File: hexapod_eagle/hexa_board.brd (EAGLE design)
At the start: 80 x 90 mm, 68 parts, among them X1 ARK2, X2 ARK1

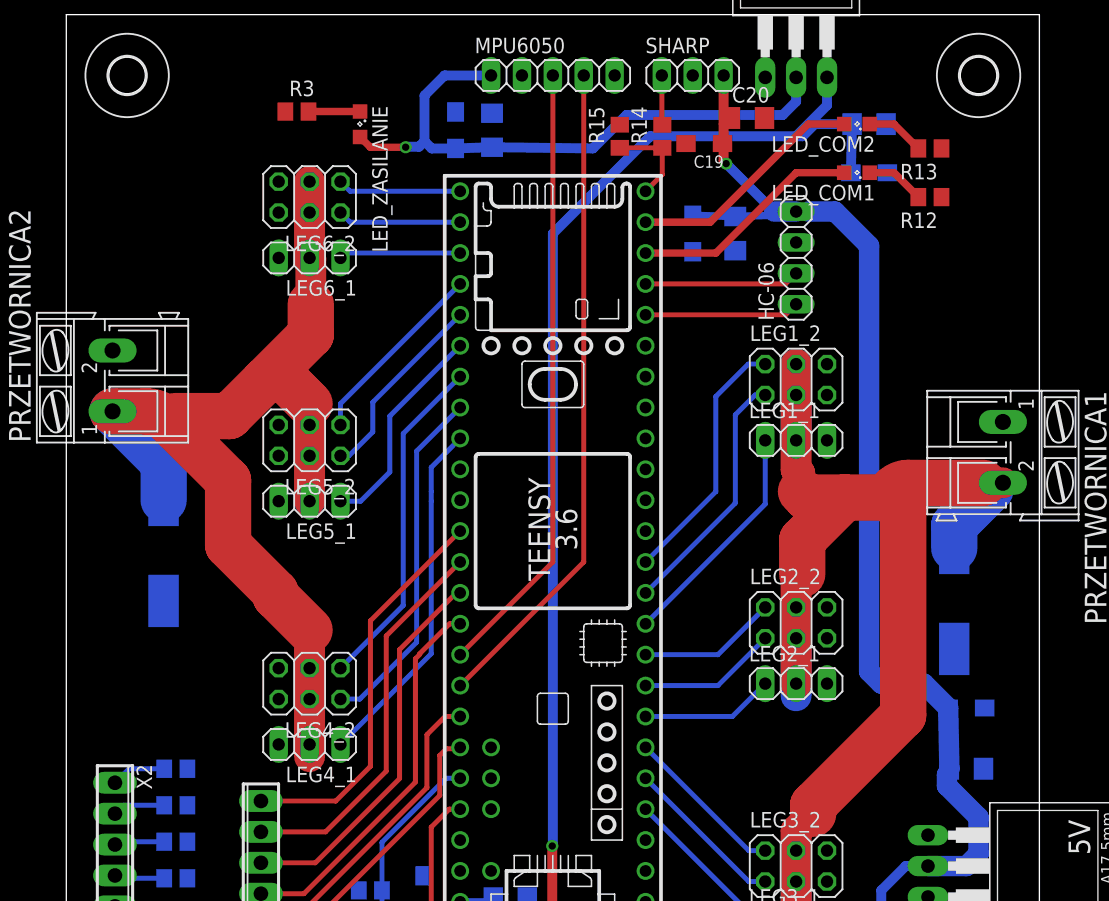
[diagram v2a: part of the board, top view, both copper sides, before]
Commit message: Update eagle files
-change positions some capacitors
-change TXD/RXD lines
-minor changes
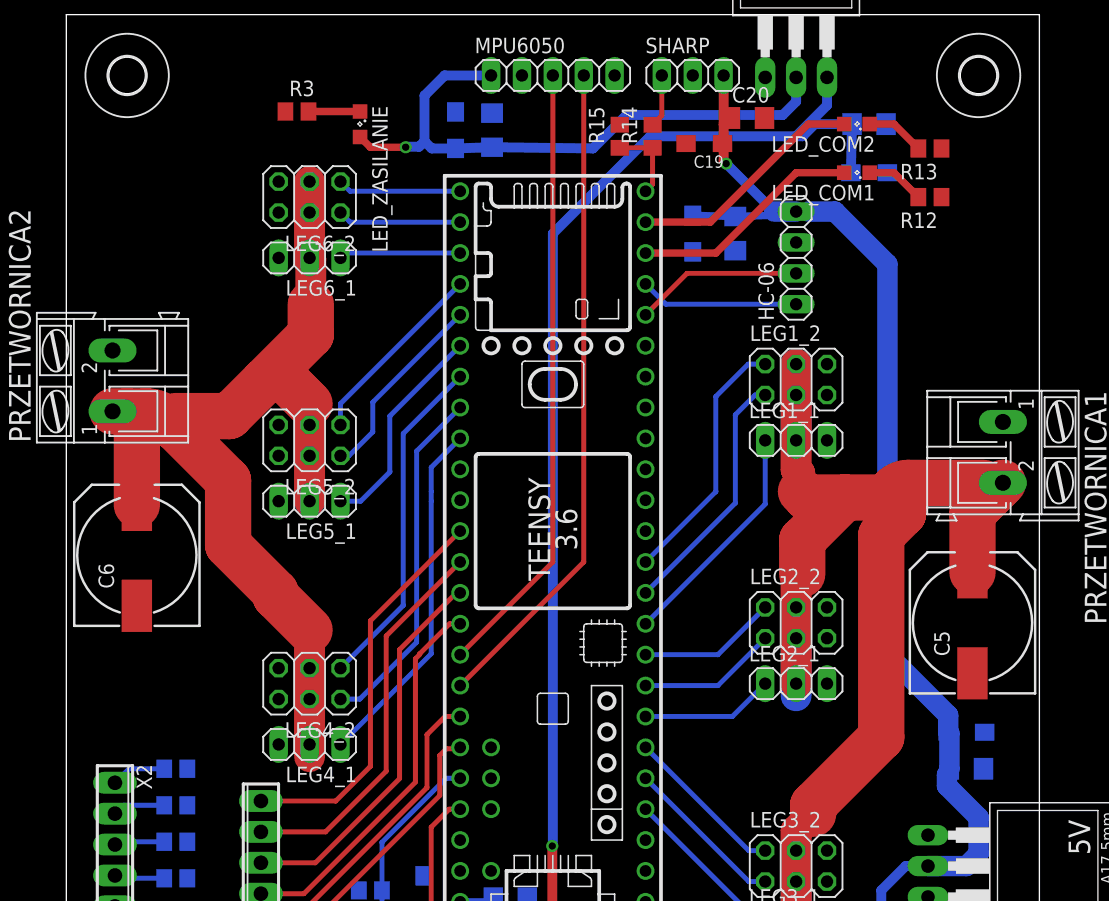
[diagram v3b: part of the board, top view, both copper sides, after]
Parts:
- moved C5 2.50 mm to (34.5, -5.00), flipped to the top
- moved C6 2.24 mm to (-34.2, 0.55), flipped to the top
- moved C4 2.00 mm to (34.0, -14.0)
- moved R14 0.80 mm to (8.20, 35.0)
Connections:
- net RXD7: now also TEENSY41.28; no longer TEENSY41.29
- net TXD7: now also TEENSY41.29; no longer TEENSY41.28
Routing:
- net +6V1: track 146.8 -> 149.1 mm
- net +5V: track 118.7 -> 116.7 mm
- net SENSOR: track 7.64 -> 6.51 mm
- net RXD7: track 12.7 -> 13.8 mm
- net +6V2: track 104.7 -> 103.6 mm
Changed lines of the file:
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@@
 <grid distance="1" unitdist="mm" unit="mm" style="lines" multiple="1" display="no" altdistance="0.05" altunitdist="mm" altunit="mm"/>
 <layers>
-<layer number="1" name="Top" color="4" fill="1" visible="yes" active="yes"/>
+<layer number="1" name="Top" color="4" fill="1" visible="no" active="yes"/>
 <layer number="2" name="Route2" color="1" fill="3" visible="no" active="no"/>
 <layer number="3" name="Route3" color="4" fill="3" visible="no" active="no"/>
@@
 <element name="C2" library="rcl" package="C1206" value="10uF" x="34" y="-31"/>
 <element name="C3" library="rcl" package="C1206" value="10uF" x="34" y="-17" rot="MR180"/>
-<element name="C4" library="rcl" package="SMC_A" value="100n" x="34" y="-12" rot="MR180"/>
+<element name="C4" library="rcl" package="SMC_A" value="100n" x="34" y="-14" rot="MR180"/>
 <element name="HC-06" library="pinhead" package="1X04" value="" x="20" y="25" rot="R90"/>
 <element name="R1" library="rcl" package="R0805" value="510r" x="-8" y="-33"/>
@@
 <attribute name="OC_FARNELL" value="unknown" x="-36" y="-24.5" size="1.778" layer="27" rot="R270" display="off"/>
 </element>
-<element name="C5" library="rcl" package="150CLZ-1014" value="" x="33" y="-3" rot="MR90"/>
-<element name="C6" library="rcl" package="150CLZ-1014" value="" x="-32" y="0.95" rot="MR90"/>
+<element name="C5" library="rcl" package="150CLZ-1014" value="" x="34.5" y="-5" rot="R90"/>
+<element name="C6" library="rcl" package="150CLZ-1014" value="" x="-34.2" y="0.55" rot="R90"/>
 <element name="WLACZNIK1" library="switch" package="255SB" value="7.2V" x="16" y="-41.7"/>
 <element name="C11" library="rcl" package="SMC_A" value="100n" x="-10.6" y="-27.3" rot="MR90"/>
@@
 <element name="C15" library="rcl" package="SMC_A" value="100n" x="11.5" y="27" rot="MR270"/>
 <element name="C16" library="rcl" package="C1206" value="10uF" x="15" y="27" rot="MR270"/>
-<element name="R14" library="rcl" package="R0805" value="510r" x="9" y="35" rot="R90"/>
+<element name="R14" library="rcl" package="R0805" value="510r" x="8.2" y="35" rot="R90"/>
 <element name="R15" library="rcl" package="R0805" value="510r" x="5.5" y="35" rot="R90"/>
 <element name="C17" library="rcl" package="C1206" value="10uF" x="20.45" y="-37.25" rot="MR225"/>
@@
 <wire x1="20" y1="-22.1" x2="21.4" y2="-20.7" width="2.54" layer="1"/>
 <wire x1="21.4" y1="-20.7" x2="21.4" y2="-20" width="3.81" layer="1"/>
-<wire x1="21.4" y1="-20" x2="28.8" y2="-12.6" width="3.81" layer="1"/>
-<wire x1="28.8" y1="-12.6" x2="28.8" y2="4" width="3.81" layer="1"/>
 <wire x1="28.8" y1="4" x2="28.8" y2="4.8" width="3.81" layer="1"/>
 <wire x1="28.8" y1="4.8" x2="29" y2="5" width="3.81" layer="1"/>
@@
 <wire x1="28.74395" y1="4.05605" x2="28.8" y2="4" width="3.81" layer="1"/>
 <contactref element="C5" pad="+"/>
-<wire x1="33" y1="1.15" x2="33" y2="3" width="3.81" layer="16"/>
-<wire x1="33" y1="3" x2="36" y2="6" width="3.81" layer="16"/>
-<wire x1="35.426075" y1="6.5108" x2="36" y2="6" width="0" layer="19" extent="1-16"/>
+<wire x1="28.8" y1="4" x2="27" y2="2.2" width="3.81" layer="1"/>
+<wire x1="27" y1="2.2" x2="27" y2="-14.4" width="3.81" layer="1"/>
+<wire x1="21.4" y1="-20" x2="27" y2="-14.4" width="3.81" layer="1"/>
+<wire x1="37" y1="6.5108" x2="34.5" y2="4.0108" width="3.81" layer="1"/>
+<wire x1="34.5" y1="4.0108" x2="34.5" y2="-0.85" width="3.81" layer="1"/>
 </signal>
 <signal name="+6V2">
@@
 <wire x1="-19.9" y1="24.9" x2="-20" y2="25" width="2.54" layer="1"/>
 <contactref element="PRZETWORNICA2" pad="1"/>
-<wire x1="-36.2" y1="12.3854" x2="-33.437503125" y2="12.3854" width="3.81" layer="1"/>
+<wire x1="-36.2" y1="12.3854" x2="-35" y2="12.3854" width="3.81" layer="1"/>
+<wire x1="-35" y1="12.3854" x2="-33.437503125" y2="12.3854" width="3.81" layer="1"/>
 <wire x1="-33.437503125" y1="12.3854" x2="-31.64145" y2="11.64145" width="3.81" layer="1" curve="-45.00005"/>
 <wire x1="-31.64145" y1="11.64145" x2="-31" y2="11" width="3.81" layer="1"/>
 <contactref element="C6" pad="+"/>
-<wire x1="-32" y1="5.1" x2="-32" y2="8.1854" width="3.81" layer="16"/>
-<wire x1="-32" y1="8.1854" x2="-36.2" y2="12.3854" width="3.81" layer="16"/>
+<wire x1="-34.2" y1="4.7" x2="-34.2" y2="11.5854" width="3.81" layer="1"/>
+<wire x1="-34.2" y1="11.5854" x2="-35" y2="12.3854" width="3.81" layer="1"/>
 </signal>
 <signal name="SDA">
@@
 <wire x1="21" y1="28.81" x2="23.19" y2="28.81" width="1.6764" layer="16"/>
 <contactref element="5V" pad="2"/>
-<wire x1="32.5" y1="-12" x2="32.6" y2="-17" width="1.6764" layer="16"/>
 <contactref element="SHARP" pad="3"/>
 <wire x1="14.04" y1="40" x2="14.04" y2="36" width="0.8128" layer="1"/>
@@
 <wire x1="32.4" y1="-17.5" x2="32.5" y2="-17.4" width="1.6764" layer="16"/>
 <wire x1="32.5" y1="-17.4" x2="32.6" y2="-17" width="1.6764" layer="16"/>
-<wire x1="32.5" y1="-12" x2="30.5" y2="-10" width="1.6764" layer="16"/>
-<wire x1="30.5" y1="-10" x2="27" y2="-10" width="1.6764" layer="16"/>
-<wire x1="27" y1="-10" x2="26" y2="-9" width="1.6764" layer="16"/>
-<wire x1="26" y1="-9" x2="26" y2="26" width="1.6764" layer="16"/>
-<wire x1="26" y1="26" x2="23.19" y2="28.81" width="1.6764" layer="16"/>
+<wire x1="27.5" y1="24.5" x2="23.19" y2="28.81" width="1.6764" layer="16"/>
 <contactref element="WLACZNIK1" pad="2"/>
 <contactref element="C15" pad="+"/>
@@
 <wire x1="14.04" y1="34.3" x2="13.95" y2="34.3" width="0.4064" layer="1"/>
 <wire x1="13.95" y1="34.3" x2="13.95" y2="34.4" width="0.4064" layer="1"/>
+<wire x1="32.6" y1="-17" x2="32.6" y2="-14.1" width="1.6764" layer="16"/>
+<wire x1="32.6" y1="-14.1" x2="32.5" y2="-14" width="1.6764" layer="16"/>
+<wire x1="32.5" y1="-14" x2="32.5" y2="-12.6" width="1.6764" layer="16"/>
+<wire x1="27.5" y1="24.5" x2="27.5" y2="-7.6" width="1.6764" layer="16"/>
+<wire x1="27.5" y1="-7.6" x2="32.5" y2="-12.6" width="1.6764" layer="16"/>
 </signal>
 <signal name="LEG6">
@@
 </signal>
 <signal name="TXD7">
+<contactref element="HC-06" pad="1"/>
+<contactref element="TEENSY41" pad="29"/>
+<wire x1="7.62" y1="22.86" x2="9.29" y2="21.19" width="0.4064" layer="16"/>
+<wire x1="9.29" y1="21.19" x2="20" y2="21.19" width="0.4064" layer="16"/>
+</signal>
+<signal name="RXD7">
+<contactref element="HC-06" pad="2"/>
 <contactref element="TEENSY41" pad="28"/>
-<contactref element="HC-06" pad="1"/>
-<wire x1="7.62" y1="20.32" x2="19.13" y2="20.32" width="0.4064" layer="1"/>
-<wire x1="19.13" y1="20.32" x2="20" y2="21.19" width="0.4064" layer="1"/>
-</signal>
-<signal name="RXD7">
-<contactref element="TEENSY41" pad="29"/>
-<contactref element="HC-06" pad="2"/>
-<wire x1="7.62" y1="22.86" x2="19.13" y2="22.86" width="0.4064" layer="1"/>
-<wire x1="19.13" y1="22.86" x2="20" y2="23.73" width="0.4064" layer="1"/>
+<wire x1="7.62" y1="20.32" x2="11.03" y2="23.73" width="0.4064" layer="1"/>
+<wire x1="11.03" y1="23.73" x2="20" y2="23.73" width="0.4064" layer="1"/>
 </signal>
 <signal name="LED(BOARD)">
@@
 <contactref element="R14" pad="1"/>
 <contactref element="R15" pad="1"/>
-<wire x1="9" y1="34.05" x2="9" y2="31.86" width="0.4064" layer="1"/>
-<wire x1="9" y1="31.86" x2="7.62" y2="30.48" width="0.4064" layer="1"/>
-<wire x1="5.5" y1="34.05" x2="9" y2="34.05" width="0.4064" layer="1"/>
+<wire x1="7.62" y1="30.48" x2="8.2" y2="31.06" width="0.4064" layer="1"/>
+<wire x1="8.2" y1="31.06" x2="8.2" y2="34.05" width="0.4064" layer="1"/>
+<wire x1="5.5" y1="34.05" x2="8.2" y2="34.05" width="0.4064" layer="1"/>
 </signal>
 <signal name="+5MCU">
@@
 <contactref element="SHARP" pad="1"/>
 <contactref element="R14" pad="2"/>
-<wire x1="8.96" y1="40" x2="8.96" y2="35.99" width="0.4064" layer="1"/>
-<wire x1="8.96" y1="35.99" x2="9" y2="35.95" width="0.4064" layer="1"/>
+<wire x1="8.2" y1="35.95" x2="8.96" y2="36.71" width="0.4064" layer="1"/>
+<wire x1="8.96" y1="36.71" x2="8.96" y2="40" width="0.4064" layer="1"/>
 </signal>
 </signals>

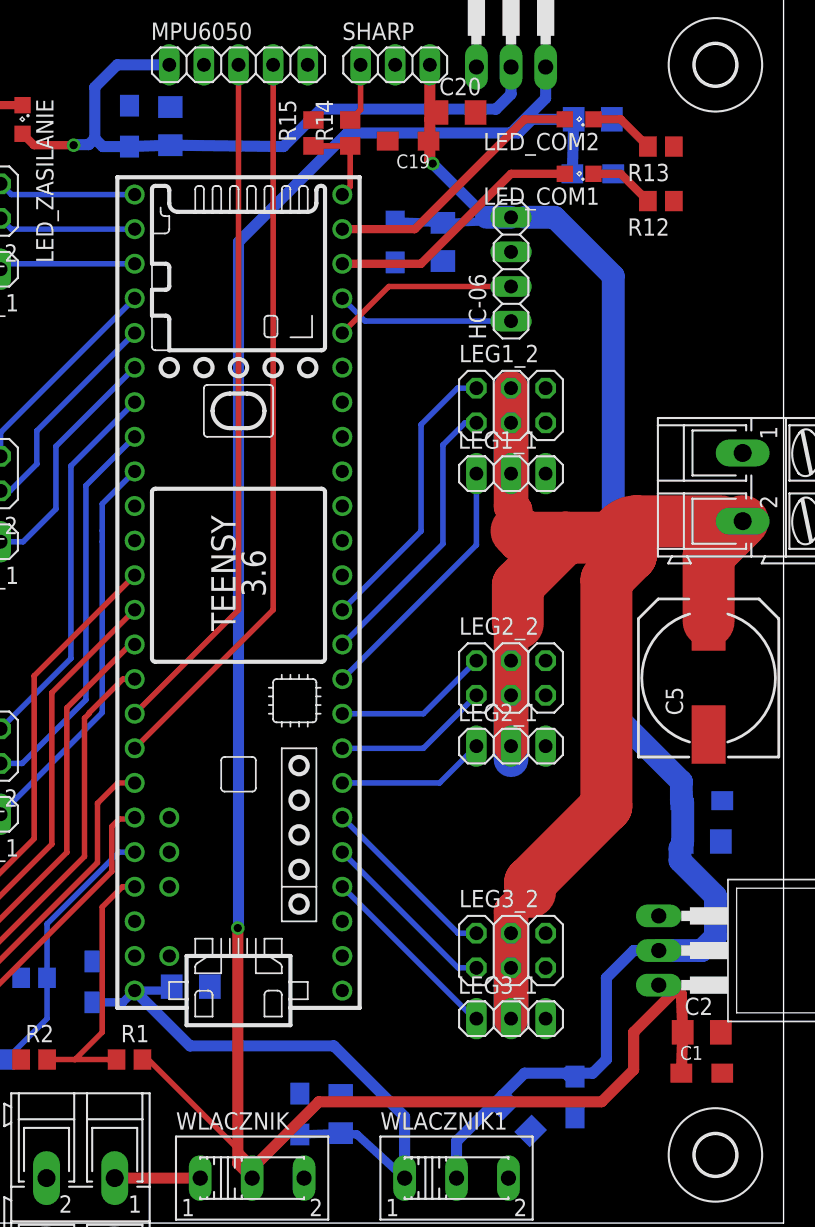
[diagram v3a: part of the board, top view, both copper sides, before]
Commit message: Update eagle files
Change some capacitors package.
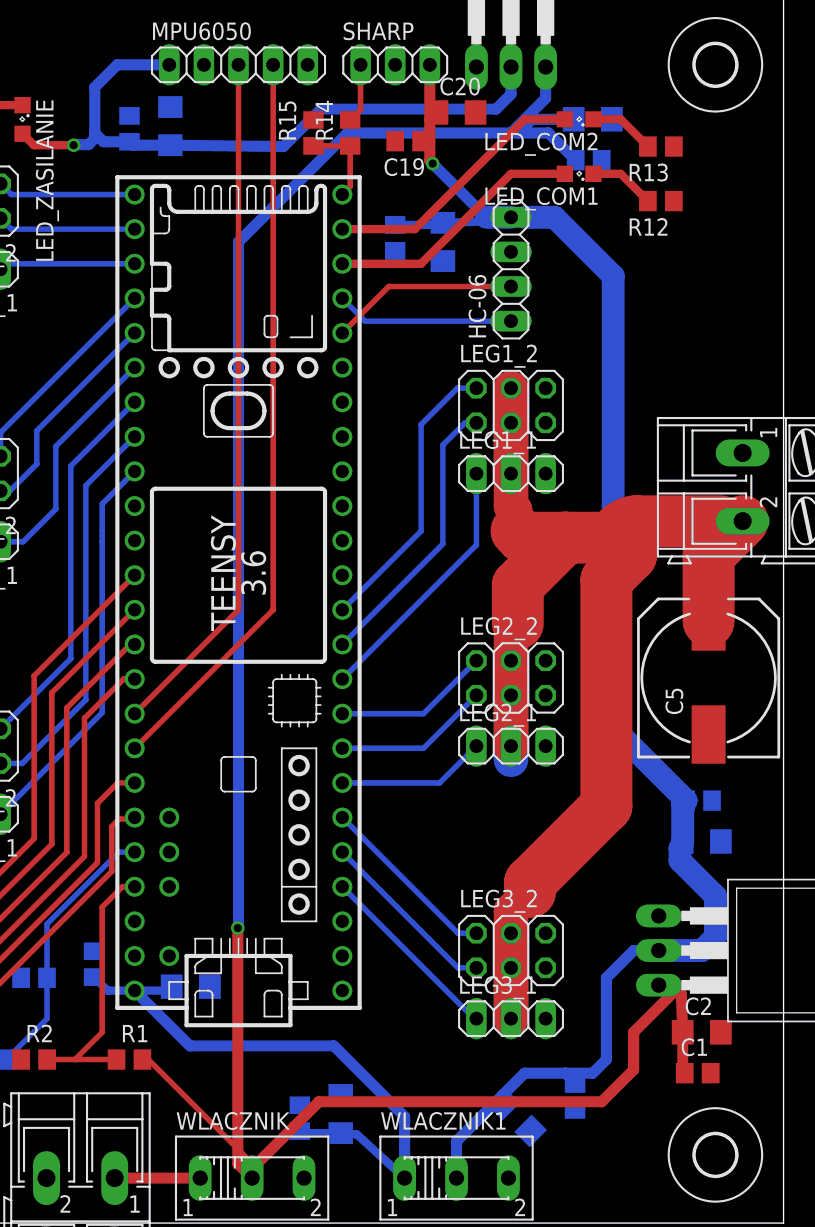
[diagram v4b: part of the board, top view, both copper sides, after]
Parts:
- C1, C10, C11, C14, C15, C18, C19, C4, C9: device rcl:SMC_A -> rcl:C0805
- moved C11 1.30 mm to (-10.6, -26.0)
- moved C9 1.04 mm to (25.7, 33.0)
- moved C15 0.30 mm to (11.5, 27.3)
- moved C1 0.30 mm to (33.7, -34.0)
- moved C14 0.30 mm to (4.50, -37.3)
- moved C10 0.20 mm to (-8.00, 35.3)
- moved C4 0.20 mm to (33.8, -14.0)
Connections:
- net +3V3: now also C10.1; no longer C10.+
- net +5MCU: now also C11.1, C14.1; no longer C11.+, C14.+
- net +5V: now also C15.1, C18.1, C19.1, C4.1; no longer C15.+, C18.+, C19.+, C4.+
- net +BAT: now also C1.1, C9.1; no longer C1.+, C9.+
- net GND: now also C1.2, C10.2, C11.2, C14.2, C15.2, C18.2, C19.2, C4.2, C9.2; no longer C1.-, C10.-, C11.-, C14.-, C15.-, C18.-, C19.-, C4.-, C9.-
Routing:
- net +BAT: track 166.2 -> 167.3 mm
- net +5V: track 116.7 -> 117.7 mm
